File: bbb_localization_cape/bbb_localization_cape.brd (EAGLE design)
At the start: 71.8 x 54.6 mm, 31 parts, among them J2 MOLEX-22-03-5035, U1 SN65HVD256DR, U2 ARDUCAMOV5642, U3 MSP430G2553IPW20R, U4 SN74LV1T126DCKR, U5 SN74LV1T125DCKR, U6 SN74LV1T126DCKR, U7 LP38693MP-3.3/NOPB, U8 LM1085ISX-ADJ

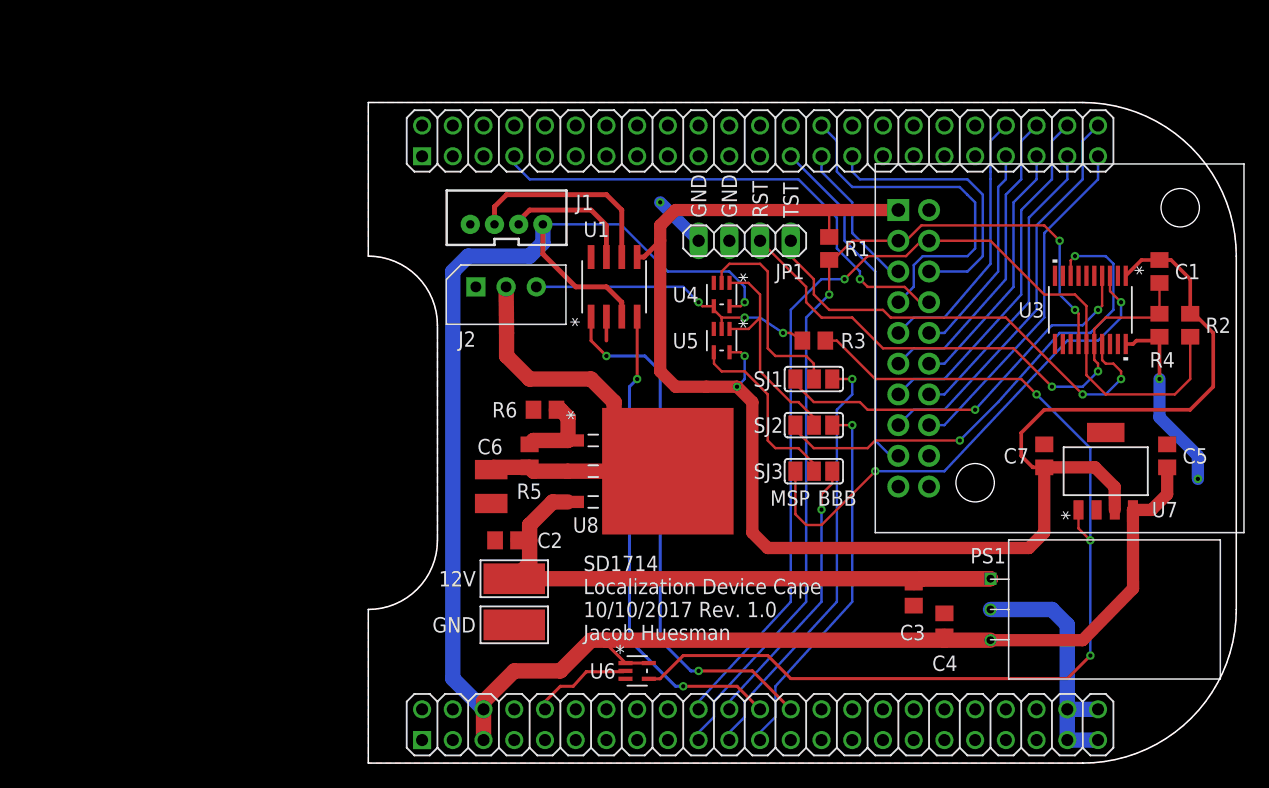
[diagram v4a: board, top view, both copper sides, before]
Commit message: Added power planes
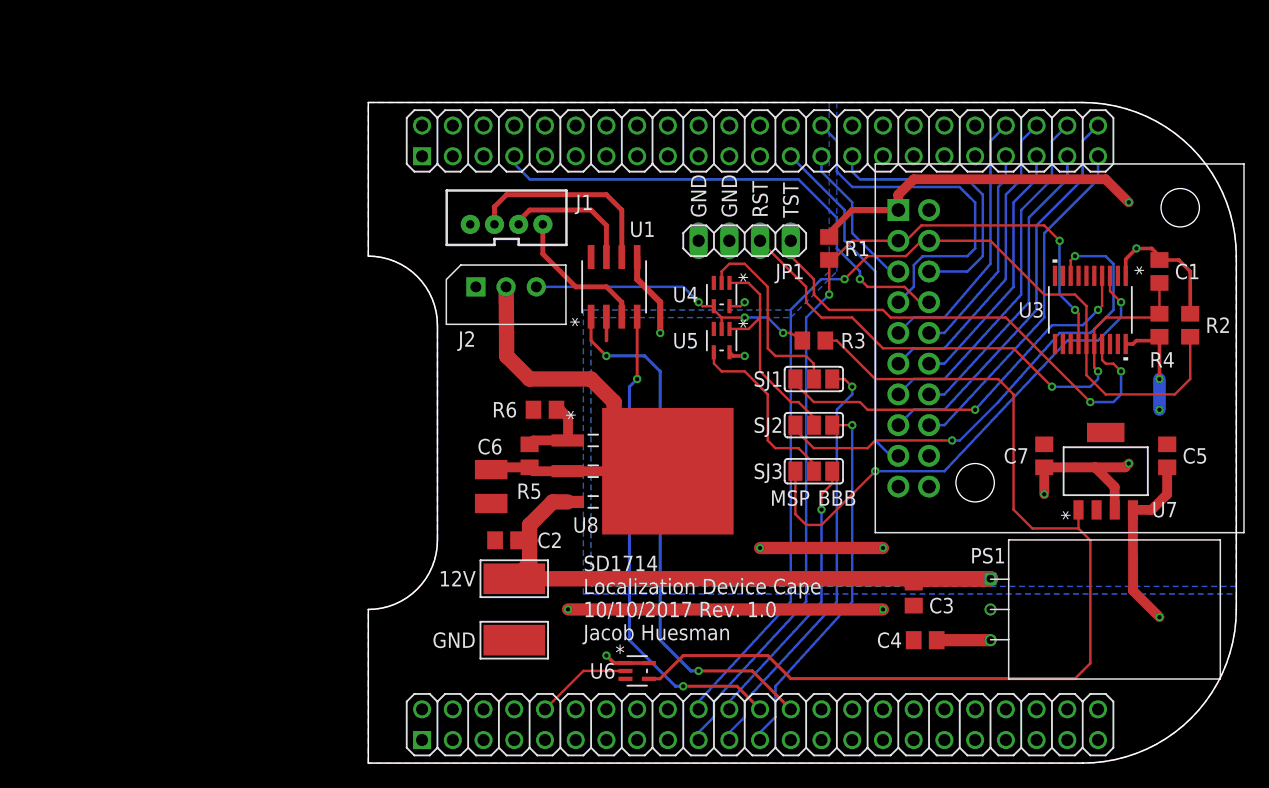
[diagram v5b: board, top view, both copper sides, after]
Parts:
- moved C4 2.03 mm to (60.6, 10.2), turned to 180 degrees
- moved PAD2 1.27 mm to (26.7, 10.2)
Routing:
- net +5V: track 158.3 -> 62.8 mm, vias 1 -> 5
- net +3V3: track 138.3 -> 72.6 mm, vias 2 -> 8
- net GND: track 44.1 -> 11.1 mm, vias 3 -> 2
- net TEST: track 38.5 -> 39.8 mm
- net UART_DYN_TXD: track 17.2 -> 16.5 mm
- net SYS_RESETN_5V: track 84.5 -> 84.6 mm, vias 3 -> 0
- added copper zone on layer 16, net +3V3
- added copper zone on layer 16, net +5V

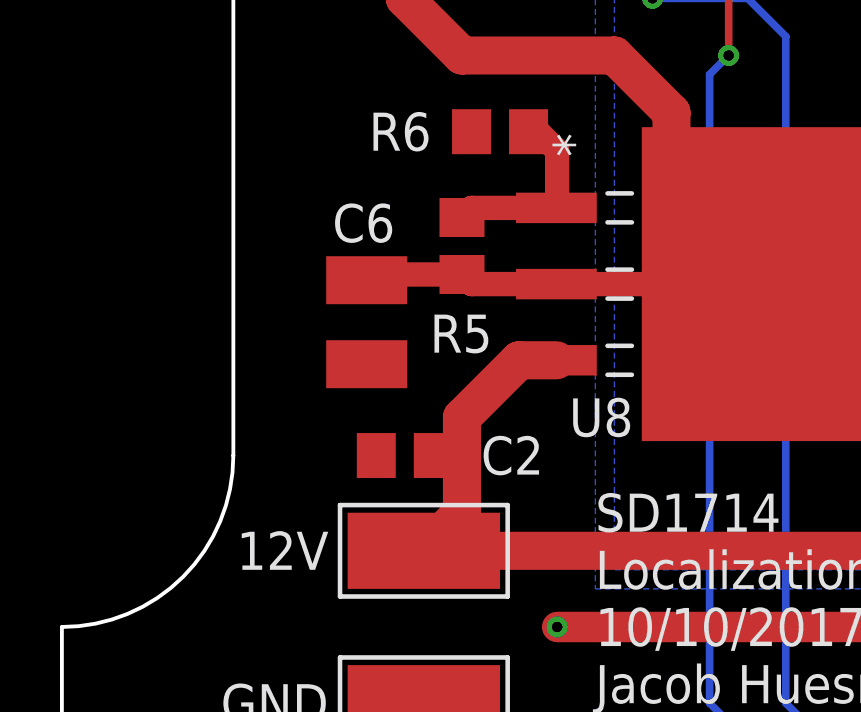
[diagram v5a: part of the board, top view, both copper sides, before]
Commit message: Began adding 3D models of components
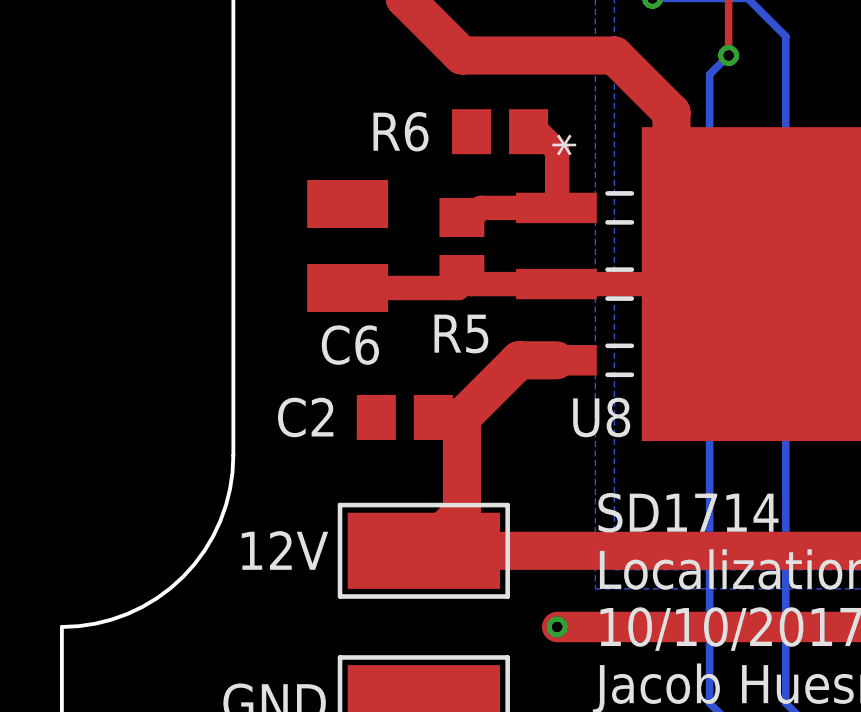
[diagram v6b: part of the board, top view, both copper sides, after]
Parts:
- R1, R2, R3, R4, R5, R6: device resistor:R0805 -> rcl:R0805
- U3: device bbb_cape_parts:PW20 -> bbb_localization_cape:PW20
- moved C6 2.62 mm to (24.1, 25.4), turned to 90 degrees
- moved C2 1.27 mm to (26.0, 19.7)
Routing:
- net +10V: track 36.8 -> 37.6 mm

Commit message: Almost done adding 3D models
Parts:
- C1, C2, C3, C4, C5, C7: device resistor:C0805 -> rcl:C0805
- C6: device resistor:C1210 -> rcl:C1206
- J1: value (none) -> CONN_04; device SparkFun-Connectors:JST-4-PTH-VERT -> bbb_localization_cape:JST-4-PTH-VERT
- PAD1, PAD2: value WIREPADSMD5-2,5 -> WIREPADSMD2,54-5,08; device wirepad:5-2,5 -> bbb_localization_cape:SMD2,54-5,08
- SJ1, SJ2, SJ3: device jumper:SJ_2 -> bbb_localization_cape:SJ_2
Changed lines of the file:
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@@
 </layers>
 <board>
-<fusionsync huburn="a.cGVyc29uYWw6dWUyYjQyNjE5" projecturn="a.cGVyc29uYWw6dWUyYjQyNjE5IzIwMTcxMDA4OTczMTc3MDE" f3durn="urn:adsk.wipprod:dm.lineage:4ue_-3ieTSSXT3ZEs_mMkw" pcbguid="aeb03dfb-aa97-4c81-a82f-a409306b356b" lastpulledtime="" lastsyncedchangeguid="afa7739a-3a94-ddd7-1908-739960551191"/>
+<fusionsync huburn="a.cGVyc29uYWw6dWUyYjQyNjE5" projecturn="a.cGVyc29uYWw6dWUyYjQyNjE5IzIwMTcxMDA4OTczMTc3MDE" f3durn="urn:adsk.wipprod:dm.lineage:4ue_-3ieTSSXT3ZEs_mMkw" pcbguid="aeb03dfb-aa97-4c81-a82f-a409306b356b" lastpulledtime="" lastsyncedchangeguid="529500f1-aa39-b450-d781-35c28706ecb8"/>
 <plain>
 <text x="71.12" y="-20.32" size="1.778" layer="48" rot="R270">Add holes for bolts</text>
@@
 </autorouter>
 <elements>
-<element name="PAD1" library="wirepad" library_urn="urn:adsk.eagle:library:412" package="5-2,5" package3d_urn="urn:adsk.eagle:package:30845/1" value="WIREPADSMD5-2,5" x="26.67" y="15.24" smashed="yes" rot="R270">
+<element name="PAD1" library="bbb_localization_cape" library_urn="urn:adsk.eagle:library:616562" package="SMD2,54-5,08" package3d_urn="urn:adsk.eagle:package:617414/2" value="WIREPADSMD2,54-5,08" x="26.67" y="15.24" smashed="yes" rot="R270">
 <attribute name="VALUE" x="29.47" y="15.34" size="0.0254" layer="27" rot="R270"/>
 </element>
@@
 <attribute name="NAME" x="67.31" y="17.78" size="1.27" layer="21" rot="R180"/>
 </element>
-<element name="PAD2" library="wirepad" library_urn="urn:adsk.eagle:library:412" package="5-2,5" package3d_urn="urn:adsk.eagle:package:30845/1" value="WIREPADSMD5-2,5" x="26.67" y="10.16" smashed="yes" rot="R270">
+<element name="PAD2" library="bbb_localization_cape" library_urn="urn:adsk.eagle:library:616562" package="SMD2,54-5,08" package3d_urn="urn:adsk.eagle:package:617414/2" value="WIREPADSMD2,54-5,08" x="26.67" y="10.16" smashed="yes" rot="R270">
 <attribute name="VALUE" x="29.47" y="10.26" size="0.0254" layer="27" rot="R270"/>
 </element>
@@
 <attribute name="VENDOR" value="Texas Instruments" x="75.565" y="24.13" size="1.778" layer="27" rot="R90" display="off"/>
 </element>
-<element name="C7" library="resistor" library_urn="urn:adsk.eagle:library:348" package="C0805" package3d_urn="urn:adsk.eagle:package:26137/1" value="4.7uF" x="70.485" y="25.4" smashed="yes" rot="R90">
+<element name="C7" library="rcl" library_urn="urn:adsk.eagle:library:334" package="C0805" package3d_urn="urn:adsk.eagle:package:23617/2" value="4.7uF" x="70.485" y="25.4" smashed="yes" rot="R90">
 <attribute name="NAME" x="69.215" y="26.035" size="1.27" layer="25" rot="R180"/>
 </element>
-<element name="C5" library="resistor" library_urn="urn:adsk.eagle:library:348" package="C0805" package3d_urn="urn:adsk.eagle:package:26137/1" value="1uF" x="80.645" y="25.4" smashed="yes" rot="R90">
+<element name="C5" library="rcl" library_urn="urn:adsk.eagle:library:334" package="C0805" package3d_urn="urn:adsk.eagle:package:23617/2" value="1uF" x="80.645" y="25.4" smashed="yes" rot="R90">
 <attribute name="NAME" x="81.915" y="24.765" size="1.27" layer="25"/>
 </element>
-<element name="C2" library="resistor" library_urn="urn:adsk.eagle:library:348" package="C0805" package3d_urn="urn:adsk.eagle:package:26137/1" value="10uF" x="26.035" y="19.685" smashed="yes" rot="R180">
+<element name="C2" library="rcl" library_urn="urn:adsk.eagle:library:334" package="C0805" package3d_urn="urn:adsk.eagle:package:23617/2" value="10uF" x="26.035" y="19.685" smashed="yes" rot="R180">
 <attribute name="NAME" x="23.8125" y="20.32" size="1.27" layer="25" rot="R180"/>
 </element>
-<element name="C4" library="resistor" library_urn="urn:adsk.eagle:library:348" package="C0805" package3d_urn="urn:adsk.eagle:package:26137/1" value="22uF" x="60.6425" y="10.16" smashed="yes" rot="R180">
+<element name="C4" library="rcl" library_urn="urn:adsk.eagle:library:334" package="C0805" package3d_urn="urn:adsk.eagle:package:23617/2" value="22uF" x="60.6425" y="10.16" smashed="yes" rot="R180">
 <attribute name="NAME" x="58.7375" y="10.795" size="1.27" layer="25" rot="R180"/>
 </element>
-<element name="C6" library="resistor" library_urn="urn:adsk.eagle:library:348" package="C1210" package3d_urn="urn:adsk.eagle:package:26139/1" value="100uF" x="24.13" y="25.4" smashed="yes" rot="R90">
+<element name="C6" library="rcl" library_urn="urn:adsk.eagle:library:334" package="C1206" package3d_urn="urn:adsk.eagle:package:23618/2" value="100uF" x="24.13" y="25.4" smashed="yes" rot="R90">
 <attribute name="NAME" x="25.273" y="22.733" size="1.27" layer="25" rot="R180"/>
 </element>
-<element name="C3" library="resistor" library_urn="urn:adsk.eagle:library:348" package="C0805" package3d_urn="urn:adsk.eagle:package:26137/1" value="10uF" x="59.69" y="13.97" smashed="yes" rot="R270">
+<element name="C3" library="rcl" library_urn="urn:adsk.eagle:library:334" package="C0805" package3d_urn="urn:adsk.eagle:package:23617/2" value="10uF" x="59.69" y="13.97" smashed="yes" rot="R270">
 <attribute name="NAME" x="60.96" y="12.3825" size="1.27" layer="25"/>
 </element>
@@
 <attribute name="NAME" x="81.28" y="33.9725" size="1.27" layer="25" rot="R180"/>
 </element>
-<element name="C1" library="resistor" library_urn="urn:adsk.eagle:library:348" package="C0805" package3d_urn="urn:adsk.eagle:package:26137/1" value="100nF" x="80.01" y="36.195" smashed="yes" rot="R270">
+<element name="C1" library="rcl" library_urn="urn:adsk.eagle:library:334" package="C0805" package3d_urn="urn:adsk.eagle:package:23617/2" value="100nF" x="80.01" y="36.195" smashed="yes" rot="R270">
 <attribute name="NAME" x="81.28" y="40.005" size="1.27" layer="25"/>
 </element>
@@
 <attribute name="VENDOR" value="Texas Instruments" x="18.415" y="39.37" size="1.778" layer="27" rot="R90" display="off"/>
 </element>
-<element name="J1" library="SparkFun-Connectors" library_urn="urn:adsk.eagle:library:513" package="JST-4-PTH-VERT" package3d_urn="urn:adsk.eagle:package:38102/1" value="" x="26.035" y="45.085" smashed="yes">
-<attribute name="PROD_ID" value="CONN-13251" x="26.035" y="36.195" size="1.778" layer="27" display="off"/>
+<element name="J1" library="bbb_localization_cape" library_urn="urn:adsk.eagle:library:616562" package="JST-4-PTH-VERT" package3d_urn="urn:adsk.eagle:package:617428/2" value="CONN_04" x="26.035" y="45.085" smashed="yes">
 <attribute name="VALUE" x="24.384" y="41.783" size="0.6096" layer="27" font="vector" ratio="20"/>
 </element>
@@
 <attribute name="NAME" x="83.82" y="35.56" size="1.27" layer="25"/>
 </element>
-<element name="SJ3" library="jumper" library_urn="urn:adsk.eagle:library:252" package="SJ_2" package3d_urn="urn:adsk.eagle:package:15474/1" value="" x="51.435" y="24.13" smashed="yes">
+<element name="SJ3" library="bbb_localization_cape" library_urn="urn:adsk.eagle:library:616562" package="SJ_2" package3d_urn="urn:adsk.eagle:package:617412/2" value="" x="51.435" y="24.13" smashed="yes">
 <attribute name="VALUE" x="51.3349" y="24.13" size="0.02" layer="27"/>
 </element>
-<element name="SJ1" library="jumper" library_urn="urn:adsk.eagle:library:252" package="SJ_2" package3d_urn="urn:adsk.eagle:package:15474/1" value="" x="51.435" y="31.75" smashed="yes">
+<element name="SJ1" library="bbb_localization_cape" library_urn="urn:adsk.eagle:library:616562" package="SJ_2" package3d_urn="urn:adsk.eagle:package:617412/2" value="" x="51.435" y="31.75" smashed="yes">
 <attribute name="VALUE" x="51.3349" y="31.75" size="0.02" layer="27"/>
 </element>
-<element name="SJ2" library="jumper" library_urn="urn:adsk.eagle:library:252" package="SJ_2" package3d_urn="urn:adsk.eagle:package:15474/1" value="" x="51.435" y="27.94" smashed="yes">
+<element name="SJ2" library="bbb_localization_cape" library_urn="urn:adsk.eagle:library:616562" package="SJ_2" package3d_urn="urn:adsk.eagle:package:617412/2" value="" x="51.435" y="27.94" smashed="yes">
 <attribute name="VALUE" x="51.3349" y="27.94" size="0.02" layer="27"/>
 </element>
